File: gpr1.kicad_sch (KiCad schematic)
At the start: 8 parts, among them U16 74HCT541, U17 74HCT00, U18 74HCT04, U7 74HCT574

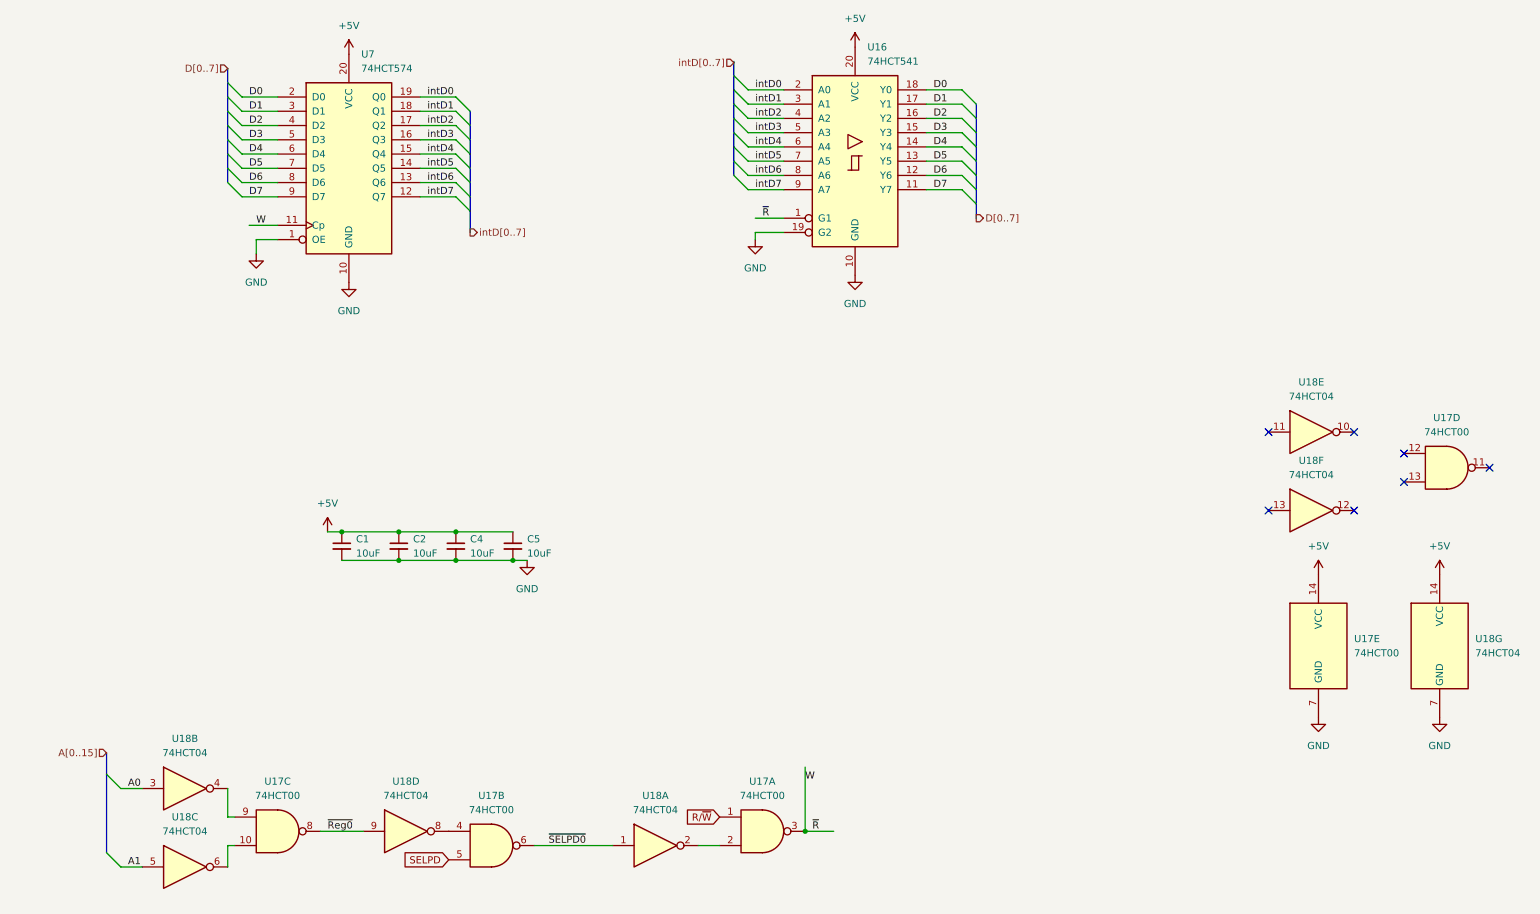
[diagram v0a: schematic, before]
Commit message: disambiguate register address
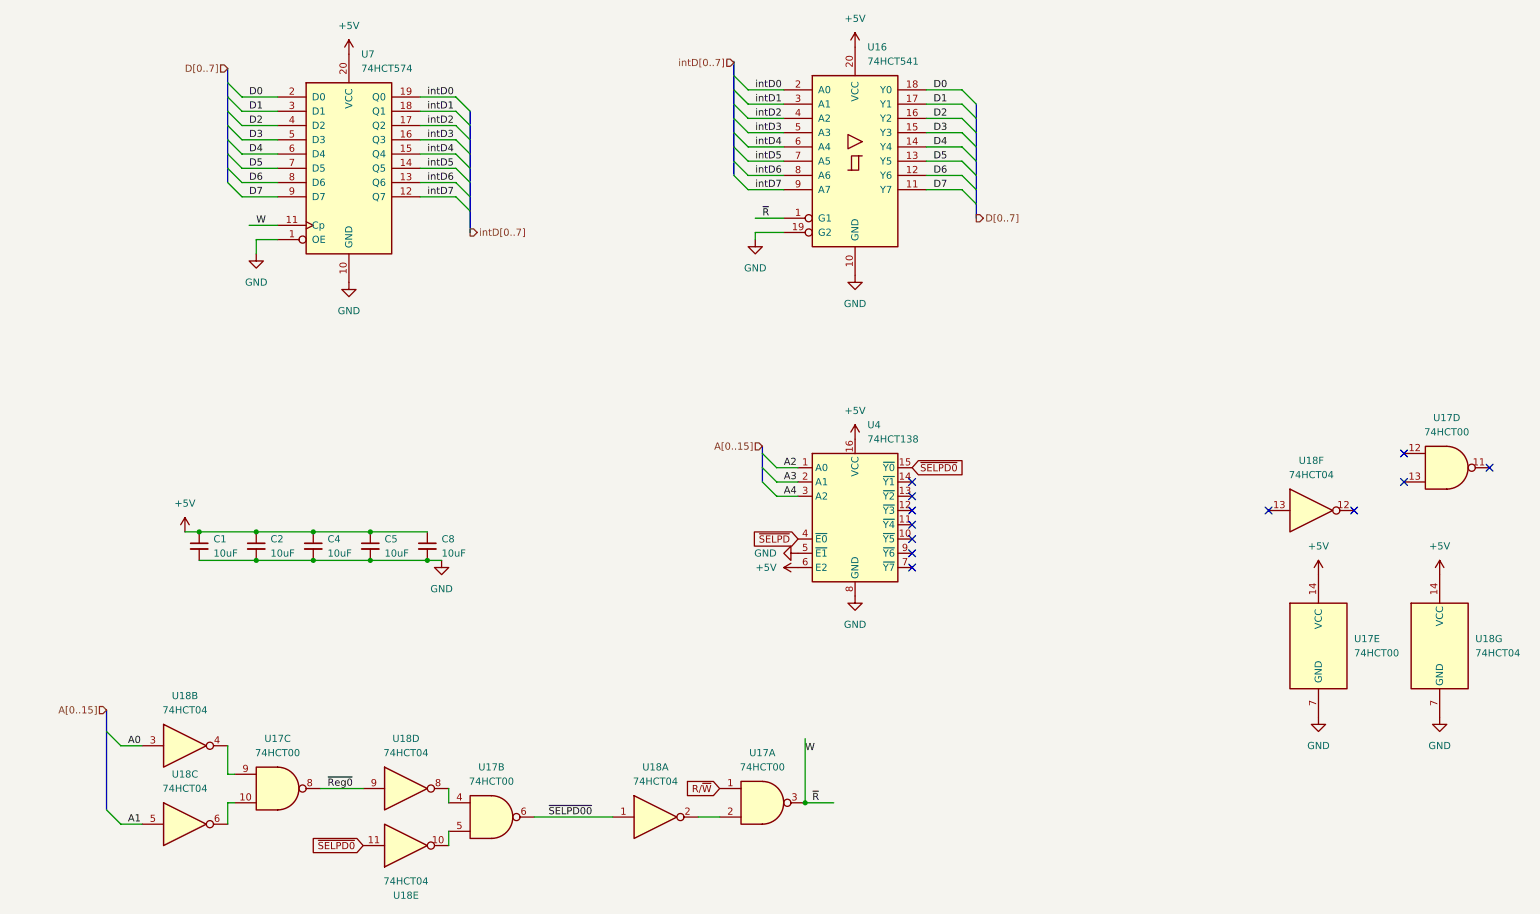
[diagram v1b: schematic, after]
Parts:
- added C8: 10uF, Capacitor_SMD:C_0805_2012Metric_Pad1.18x1.45mm_HandSolder, symbol Device:C_Small
- added U4: 74HCT138, Package_SO:SOIC-16_3.9x9.9mm_P1.27mm, symbol 74xx:74HCT138
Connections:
- net SELPD is gone; now on an unnamed net: U17.5
- net +5V: now also C8.1, U4.16 (VCC), U4.6 (E2)
- net GND: now also C8.2, U4.5 (~{E1}), U4.8 (GND)
- net ~{SELPD0}: now also U18.11, U4.15 (~{Y0}); no longer U17.6, U18.1
- new net A2: U4.1 (A0)
- new net A3: U4.2 (A1)
- new net A4: U4.3 (A2)
- new net ~{SELPD00}: U17.6, U18.1
- new net ~{SELPD}: U4.4 (~{E0})
- no-connect marks 7 -> 12
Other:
- moved on the sheet: C1, C2, C4, C5, U17A, U17B, U17C, U18A, U18B, U18C, U18D, U18E

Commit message: tighten up tracing
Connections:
- net ~{SELPD5}: now reaches U4.10 (~{Y5})
- net ~{SELPD4}: now reaches U4.11 (~{Y4})
- net ~{SELPD3}: now reaches U4.12 (~{Y3})
- net ~{SELPD2}: now reaches U4.13 (~{Y2})
- net ~{SELPD1}: now reaches U4.14 (~{Y1})
- net ~{SELPD7}: now reaches U4.7 (~{Y7})
- net ~{SELPD6}: now reaches U4.9 (~{Y6})
- no-connect marks 12 -> 5
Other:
- moved on the sheet: U16, U7

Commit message: clean up before redesign
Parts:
- removed U17: 74HCT00, Package_SO:SOIC-14_3.9x8.7mm_P1.27mm, symbol 74xx:74HCT00
- removed U18: 74HCT04, Package_SO:SOIC-14_3.9x8.7mm_P1.27mm, symbol 74xx:74HCT04
- added C10, C9: 10uF, Capacitor_SMD:C_0805_2012Metric_Pad1.18x1.45mm_HandSolder, symbol Device:C_Small
- added J6: PD0, Connector_PinSocket_2.54mm:PinSocket_1x08_P2.54mm_Vertical, symbol Connector:Conn_01x08_Socket
- added J7: PD1, Connector_PinSocket_2.54mm:PinSocket_1x08_P2.54mm_Vertical, symbol Connector:Conn_01x08_Socket
- added U5: GAL16V8, Package_DIP:DIP-20_W7.62mm, symbol Logic_Programmable:GAL16V8
- added U6: 74HCT574, Package_SO:SOIC-20W_7.5x12.8mm_P1.27mm, symbol 74xx:74LS574
- added U8: 74HCT541, Package_SO:SOIC-20W_7.5x12.8mm_P1.27mm, symbol 74xx:74LS541
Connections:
- net +5V: now also C10.1, C9.1, U5.20 (VCC), U6.20 (VCC), U8.20 (VCC)
- net A0: now also U5.1 (I1/CLK)
- net A1: now also U5.2 (I2)
- net D0: now also U6.2 (D0), U8.18 (Y0)
- net D1: now also U6.3 (D1), U8.17 (Y1)
- net D2: now also U6.4 (D2), U8.16 (Y2)
- net D3: now also U6.5 (D3), U8.15 (Y3)
- net D4: now also U6.6 (D4), U8.14 (Y4)
- net D5: now also U6.7 (D5), U8.13 (Y5)
- net D6: now also U6.8 (D6), U8.12 (Y6)
- net D7: now also U6.9 (D7), U8.11 (Y7)
- net GND: now also C10.2, C9.2, U5.10 (GND), U6.1 (OE), U6.10 (GND), U8.10 (GND), U8.19 (G2)
- net R/~{W}: now also U5.9 (I9)
- net ~{SELPD0}: now also U5.3 (I3)
- net W renamed W0
- net W0: now also U5.18 (IO2); no longer U16.1 (G1)
- net intD0 renamed intD00
- net intD00: now also J6.1 (Pin_1)
- net intD1 renamed intD01
- net intD01: now also J6.2 (Pin_2)
- net intD2 renamed intD02
- net intD02: now also J6.3 (Pin_3)
- net intD3 renamed intD03
- net intD03: now also J6.4 (Pin_4)
- net intD4 renamed intD04
- net intD04: now also J6.5 (Pin_5)
- net intD5 renamed intD05
- net intD05: now also J6.6 (Pin_6)
- net intD6 renamed intD06
- net intD06: now also J6.7 (Pin_7)
- net intD7 renamed intD07
- net intD07: now also J6.8 (Pin_8)
- new net E: U5.11 (I10/~{OE})
- new net W1: U5.16 (IO4), U6.11 (Cp)
- new net W2: U5.14 (IO6)
- new net W3: U5.12 (IO8)
- new net intD10: J7.1 (Pin_1), U6.19 (Q0), U8.2 (A0)
- new net intD11: J7.2 (Pin_2), U6.18 (Q1), U8.3 (A1)
- new net intD12: J7.3 (Pin_3), U6.17 (Q2), U8.4 (A2)
- new net intD13: J7.4 (Pin_4), U6.16 (Q3), U8.5 (A3)
- new net intD14: J7.5 (Pin_5), U6.15 (Q4), U8.6 (A4)
- new net intD15: J7.6 (Pin_6), U6.14 (Q5), U8.7 (A5)
- new net intD16: J7.7 (Pin_7), U6.13 (Q6), U8.8 (A6)
- new net intD17: J7.8 (Pin_8), U6.12 (Q7), U8.9 (A7)
- new net ~{R}0: U16.1 (G1), U5.19 (IO1)
- new net ~{R}1: U5.17 (I03), U8.1 (G1)
- new net ~{R}2: U5.15 (IO5)
- new net ~{R}3: U5.13 (IO7)
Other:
- moved on the sheet: C1, C2, C4, C5, C8, U4
